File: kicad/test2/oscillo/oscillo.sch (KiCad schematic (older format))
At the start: 8 parts

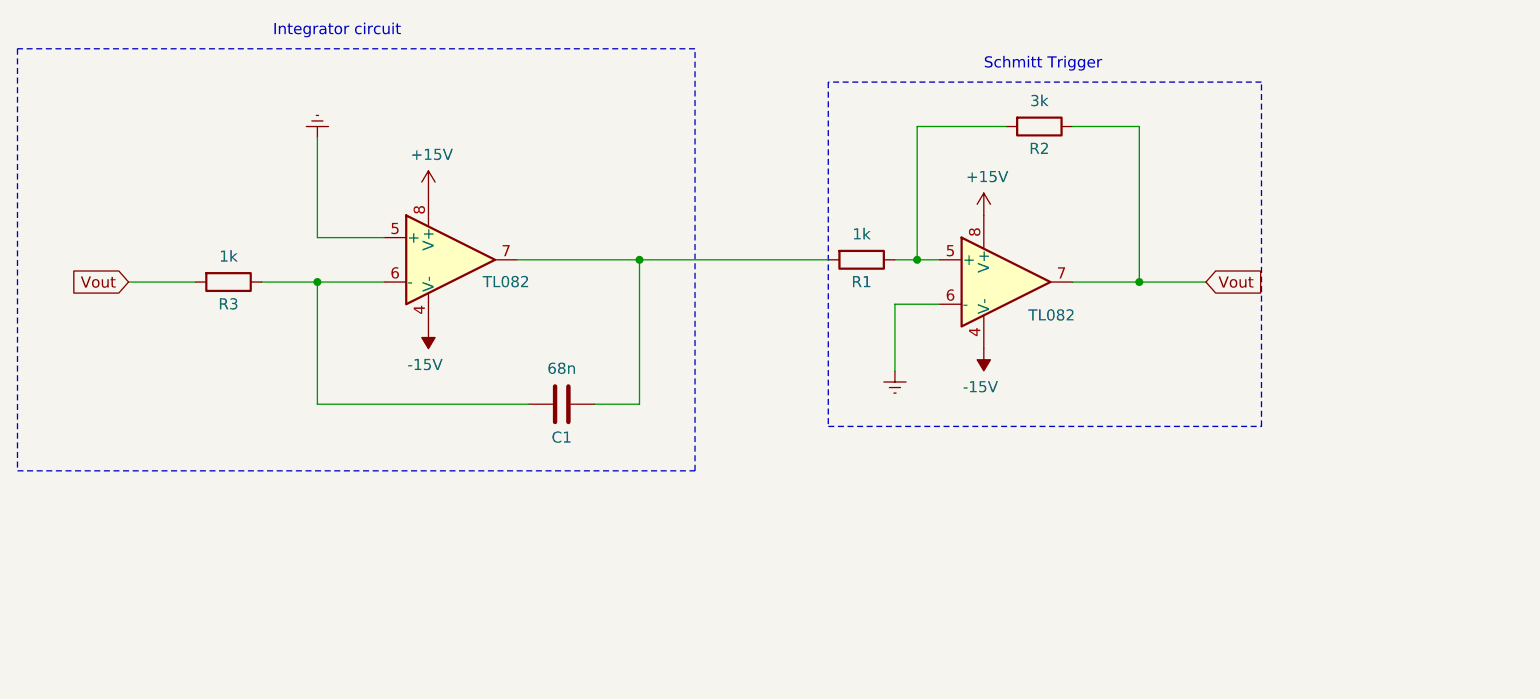
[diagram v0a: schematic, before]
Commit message: Emitter added in complete circuit
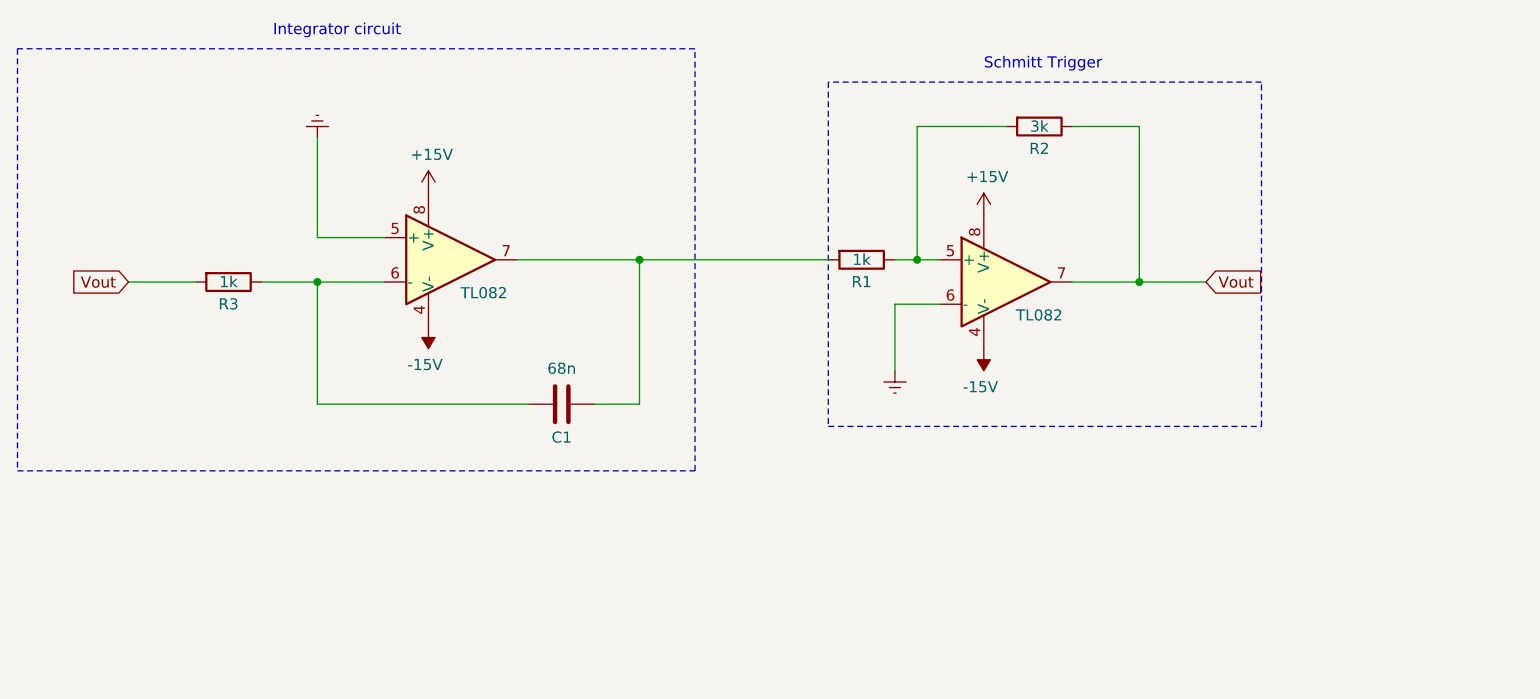
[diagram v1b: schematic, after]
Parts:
- removed U? (x3): TL082, symbol Amplifier_Operational:TL082
- removed U?: TL082, , symbol Amplifier_Operational:TL082
- added U? (x4): TL082, symbol Amplifier_Operational:TL082
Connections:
- net +15V: now also U?.8 (V+), U?.8 (V+)
- net -15V: now also U?.4 (V-), U?.4 (V-)
- net Earth: now also U?.5 (+), U?.6 (-)
- net Vout: now also U?.7
- net at C1.2, R3.1: now also U?.6 (-)
- net at C1.1, R1.2: now also U?.7
- net at R1.1, R2.2: now also U?.5 (+)
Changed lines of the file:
@@
 Comment4 ""
 $EndDescr
-$Comp
-L Amplifier_Operational:TL082 U?
-U 2 1 5E85B236
-P 4100 2500
-F 0 "U?" H 4100 2867 50  0001 C CNN
-F 1 "TL082" H 4350 2400 50  0000 C CNN
-F 2 "" H 4100 2500 50  0001 C CNN
-F 3 "http://www.ti.com/lit/ds/symlink/tl081.pdf" H 4100 2500 50  0001 C CNN
-	2    4100 2500
-	1    0    0    -1
-$EndComp
-$Comp
-L Amplifier_Operational:TL082 U?
-U 2 1 5E869437
-P 6600 2600
-F 0 "U?" H 6600 2875 50  0001 C CNN
-F 1 "TL082" H 6600 2876 50  0001 C CNN
-F 2 "" H 6600 2600 50  0001 C CNN
-F 3 "http://www.ti.com/lit/ds/symlink/tl081.pdf" H 6600 2600 50  0001 C CNN
-	2    6600 2600
-	1    0    0    -1
-$EndComp
 Wire Wire Line
 	3800 2400 3500 2400
@@
 P 3100 2600
 F 0 "R3" V 3200 2600 50  0000 C CNN
-F 1 "1k" V 2985 2600 50  0000 C CNN
+F 1 "1k" V 3100 2600 50  0000 C CNN
 F 2 "" V 3030 2600 50  0001 C CNN
 F 3 "~" H 3100 2600 50  0001 C CNN
@@
 Wire Wire Line
 	2650 2600 2950 2600
-$Comp
-L Amplifier_Operational:TL082 U?
-U 3 1 5E874865
-P 4100 2500
-F 0 "U?" H 4058 2546 50  0001 L CNN
-F 1 "TL082" H 4058 2500 50  0001 L CNN
-F 2 " " H 4100 2500 50  0001 C CNN
-F 3 "http://www.ti.com/lit/ds/symlink/tl081.pdf" H 4100 2500 50  0001 C CNN
-	3    4100 2500
-	1    0    0    -1
-$EndComp
 $Comp
 L power:Earth #PWR?
@@
 	-1   0    0    1
 $EndComp
-$Comp
-L Amplifier_Operational:TL082 U?
-U 3 1 5E877D63
-P 6600 2600
-F 0 "U?" H 6558 2646 50  0001 L CNN
-F 1 "TL082" H 6700 2450 50  0000 L CNN
-F 2 "" H 6600 2600 50  0001 C CNN
-F 3 "http://www.ti.com/lit/ds/symlink/tl081.pdf" H 6600 2600 50  0001 C CNN
-	3    6600 2600
-	1    0    0    -1
-$EndComp
 Text GLabel 2650 2600 0    50   Input ~ 0
 Vout
@@
 P 6750 1900
 F 0 "R2" V 6850 1900 50  0000 C CNN
-F 1 "3k" V 6635 1900 50  0000 C CNN
+F 1 "3k" V 6750 1900 50  0000 C CNN
 F 2 "" V 6680 1900 50  0001 C CNN
 F 3 "~" H 6750 1900 50  0001 C CNN
@@
 P 5950 2500
 F 0 "R1" V 6050 2500 50  0000 C CNN
-F 1 "1k" V 5835 2500 50  0000 C CNN
+F 1 "1k" V 5950 2500 50  0000 C CNN
 F 2 "" V 5880 2500 50  0001 C CNN
 F 3 "~" H 5950 2500 50  0001 C CNN
@@
 Text Notes 6500 1650 0    50   ~ 0
 Schmitt Trigger
-Wire Notes Line
+Wire Notes Line style dash_dot
 	2150 1550 2150 3450
-Wire Notes Line
+Wire Notes Line style dash_dot
 	2150 3450 5200 3450
-Wire Notes Line
+Wire Notes Line style dash_dot
 	5200 3450 5200 1550
-Wire Notes Line
+Wire Notes Line style dash_dot
 	5200 1550 2150 1550
 Text Notes 3300 1500 0    50   ~ 0
@@
 	1    0    0    -1
 $EndComp
+$Comp
+L Amplifier_Operational:TL082 U?
+U 3 1 5E868CF5
+P 4100 2500
+F 0 "U?" H 4058 2500 50  0001 L CNN
+F 1 "TL082" H 4058 2455 50  0001 L CNN
+F 2 "" H 4100 2500 50  0001 C CNN
+F 3 "http://www.ti.com/lit/ds/symlink/tl081.pdf" H 4100 2500 50  0001 C CNN
+	3    4100 2500
+	1    0    0    -1
+$EndComp
+$Comp
+L Amplifier_Operational:TL082 U?
+U 3 1 5E86E9A5
+P 6600 2600
+F 0 "U?" H 6558 2646 50  0001 L CNN
+F 1 "TL082" H 6558 2600 50  0001 L CNN
+F 2 "" H 6600 2600 50  0001 C CNN
+F 3 "http://www.ti.com/lit/ds/symlink/tl081.pdf" H 6600 2600 50  0001 C CNN
+	3    6600 2600
+	1    0    0    -1
+$EndComp
+$Comp
+L Amplifier_Operational:TL082 U?
+U 2 1 5E87264A
+P 4100 2500
+F 0 "U?" H 4100 2867 50  0001 C CNN
+F 1 "TL082" H 4250 2350 50  0000 C CNN
+F 2 "" H 4100 2500 50  0001 C CNN
+F 3 "http://www.ti.com/lit/ds/symlink/tl081.pdf" H 4100 2500 50  0001 C CNN
+	2    4100 2500
+	1    0    0    -1
+$EndComp
+$Comp
+L Amplifier_Operational:TL082 U?
+U 2 1 5E8755DA
+P 6600 2600
+F 0 "U?" H 6600 2967 50  0001 C CNN
+F 1 "TL082" H 6750 2450 50  0000 C CNN
+F 2 "" H 6600 2600 50  0001 C CNN
+F 3 "http://www.ti.com/lit/ds/symlink/tl081.pdf" H 6600 2600 50  0001 C CNN
+	2    6600 2600
+	1    0    0    -1
+$EndComp

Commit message: yes
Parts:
- C1: symbol Device:C -> oscillo-rescue:C-Device
- R1: value 1k -> 1K; symbol Device:R -> oscillo-rescue:R-Device
- R2: value 3k -> 8.4K; symbol Device:R -> oscillo-rescue:R-Device
- R3: value 1k -> 7.3K; symbol Device:R -> oscillo-rescue:R-Device
- U? (x4): symbol Amplifier_Operational:TL082 -> oscillo-rescue:TL082-Amplifier_Operational
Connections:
- net +15V: now also U?.~, U?.~; no longer U?.8 (V+), U?.8 (V+)
- net -15V: now also U?.~, U?.~; no longer U?.4 (V-), U?.4 (V-)
- net Earth: now also U?.~, U?.~; no longer U?.5 (+), U?.6 (-)
- net Vout: now also C1.1, R1.2, U?.~; no longer R2.1, R3.2, U?.7
- net at C1.2, R3.1: now also U?.~; no longer U?.6 (-)
- net at R1.1, R2.2: now also U?.~; no longer U?.5 (+)
- new net: R2.1, R3.2, U?.~
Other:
- moved on the sheet: C1, R1, R2, R3
